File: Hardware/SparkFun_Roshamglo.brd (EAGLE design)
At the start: 33 x 72.4 mm, 43 parts, among them IC1 ATTINY84A, J2 USBPCB, Q1 600mA/40V, U1 IR-Receiver, U3 AP2112K-3.3V

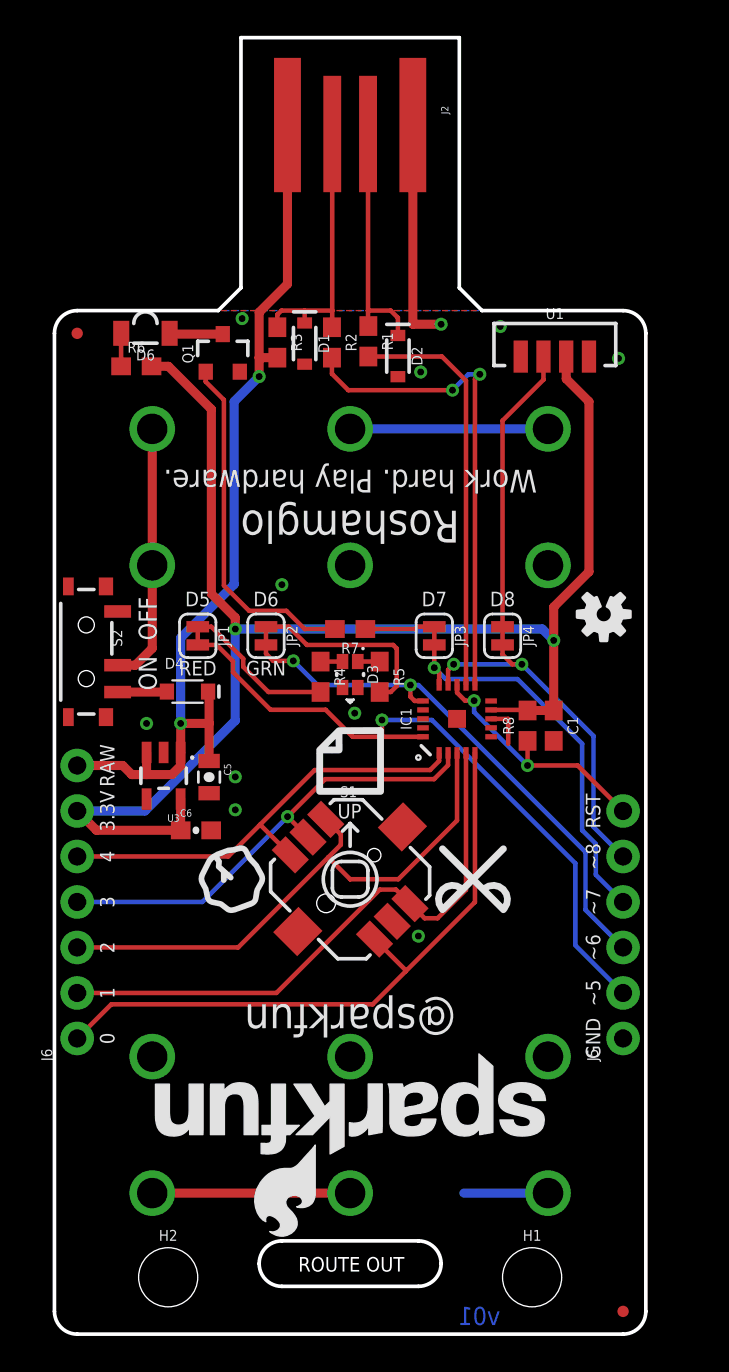
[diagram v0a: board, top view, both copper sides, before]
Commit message: v02 Changes
- Moved IR LED to GPIO 5
- Moved red and green LEDs to GPIO 7 and 8
- Moved IR receiver to GPIO 3
- Moved center switch to GPIO 6
- Increased distance between batteries
- Increased board size to 1.4"
- Added reset switch
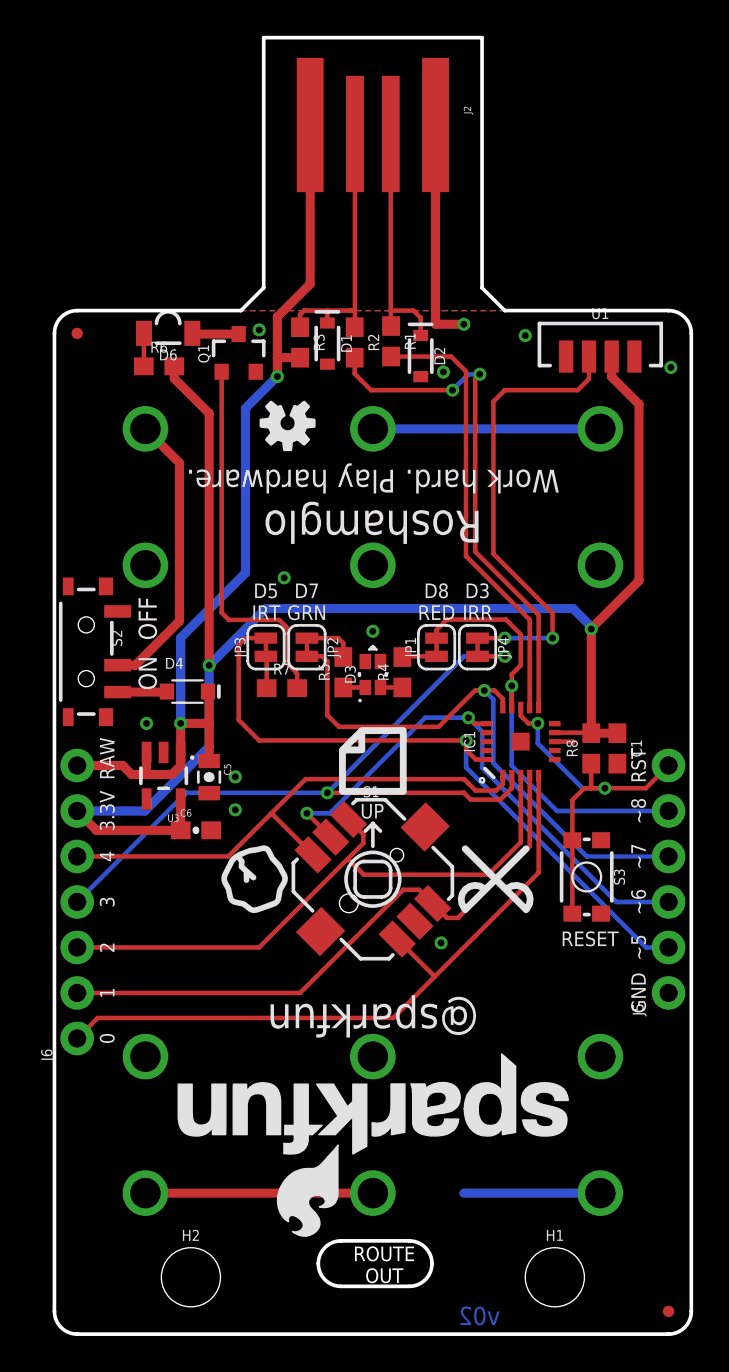
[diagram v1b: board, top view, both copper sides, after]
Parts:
- added S3: (no value), SparkFun-Switches:TACTILE_SWITCH_SMD_4.6X2.8MM
- moved LOGO1 20.6 mm to (13.0, 50.9)
- moved JP1 13.4 mm to (21.3, 38.4), turned to 90 degrees
- moved JP3 9.42 mm to (11.8, 38.4), turned to 90 degrees
- moved R7 5.04 mm to (12.7, 36.1), turned to 0 degrees
- moved R4 4.58 mm to (19.4, 37.0), turned to 90 degrees
- moved C1 3.78 mm to (31.4, 32.7)
- moved IC1 3.78 mm to (26.0, 33.1)
- moved R8 3.78 mm to (30.0, 32.7)
- moved J5 3.59 mm to (34.3, 19.1)
- moved BT3 2.92 mm to (30.5, 29.2)
- moved FD2 2.54 mm to (34.3, 1.27)
- moved U1 2.54 mm to (30.5, 55.9)
- moved JP2 2.37 mm to (14.1, 38.4)
- moved R5 2.05 mm to (16.1, 37.0), turned to 90 degrees
- moved JP4 1.53 mm to (23.6, 38.4)
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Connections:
- net !RESET: now also S3.1, S3.2
- net 3: now also JP4.2; no longer S1.CTR
- net 5: now also JP3.2; no longer JP1.2
- net 6: now also S1.CTR; no longer JP2.2
- net 7: now also JP2.2; no longer JP3.2
- net 8: now also JP1.2; no longer JP4.2
- net GND: now also S3.3, S3.4
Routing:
- net 3: track 26.2 -> 42.5 mm, vias 1 -> 2
- net 7: track 22.1 -> 32.1 mm
- net N$9: track 16.0 -> 25.9 mm, vias 0 -> 2
- net N$8: track 11.0 -> 2.96 mm
- net !RESET: track 14.2 -> 21.4 mm
- net N$7: track 8.63 -> 1.94 mm
- net 3.3V: track 84.0 -> 88.5 mm
- net 4: track 25.3 -> 29.7 mm
- net 8: track 20.0 -> 24.3 mm, vias 2 -> 1
- net 2: track 31.7 -> 34.6 mm
- net N$10: track 3.90 -> 1.82 mm
- net 9: track 23.0 -> 24.8 mm
- net 0: track 36.2 -> 38.0 mm
- net N$13: track 11.0 -> 12.7 mm
- net N$12: track 11.0 -> 12.7 mm
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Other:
- board size 33 x 72.4 mm -> 35.6 x 72.4 mm
- board text added: "D3 IRR"
- board text added: "D5 IRT"
- board text added: "D7 GRN"
- board text added: "D8 RED"
- board text added: "RESET"
- board text added: "Units are in Inches"
- board text added: "v02"
- board text removed: "D5"
- board text removed: "D6"
- board text removed: "D7"
- board text removed: "D8"
- board text removed: "GRN"
- board text removed: "RED"
- board text removed: "v01"

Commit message: Fixed V02 DRC errors
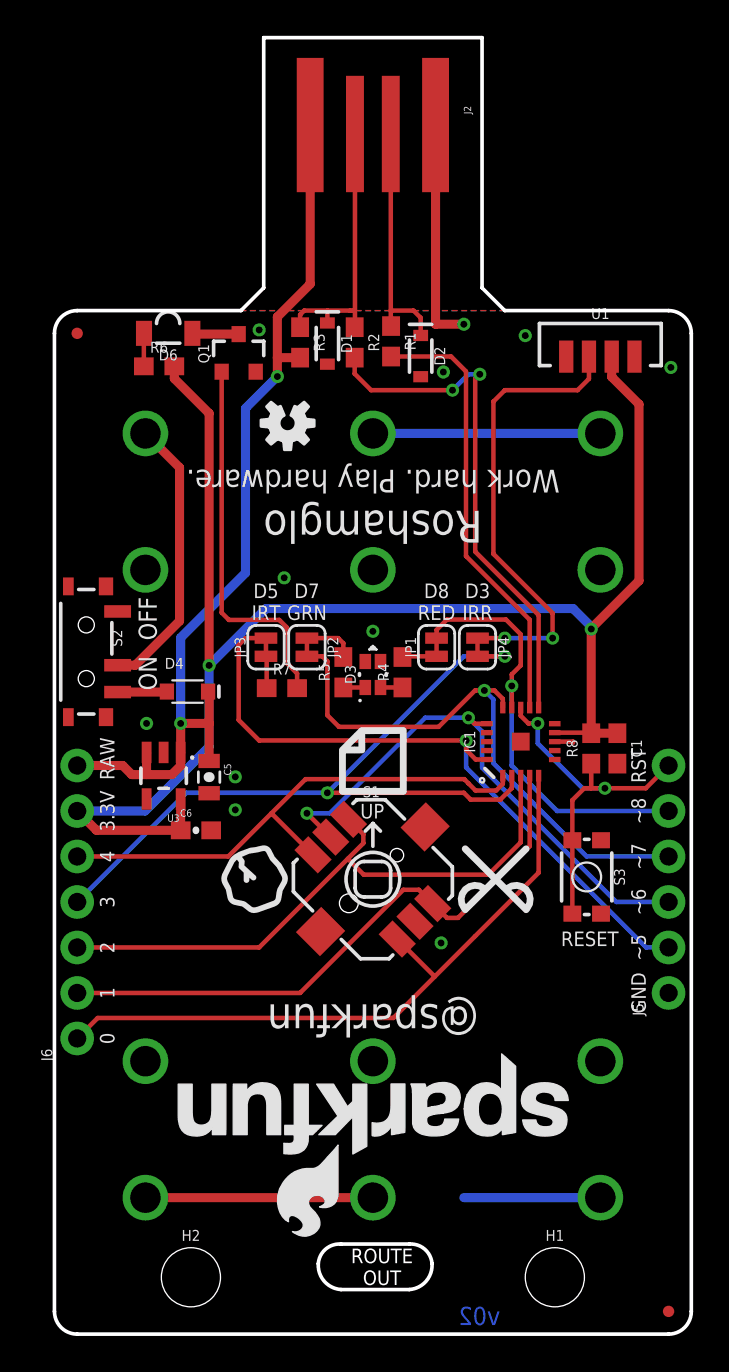
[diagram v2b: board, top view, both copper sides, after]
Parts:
- moved BT1 0.25 mm to (5.08, 29.0)
- moved BT2 0.25 mm to (17.8, 29.0)
- moved BT3 0.25 mm to (30.5, 29.0)
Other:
- outline, holes or cut-outs redrawn
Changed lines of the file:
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@@
 <layer number="31" name="tCream" color="7" fill="4" visible="no" active="yes"/>
 <layer number="32" name="bCream" color="7" fill="5" visible="no" active="yes"/>
-<layer number="39" name="tKeepout" color="4" fill="11" visible="no" active="yes"/>
-<layer number="40" name="bKeepout" color="1" fill="11" visible="no" active="yes"/>
+<layer number="39" name="tKeepout" color="4" fill="11" visible="yes" active="yes"/>
+<layer number="40" name="bKeepout" color="1" fill="11" visible="yes" active="yes"/>
 <layer number="41" name="tRestrict" color="4" fill="10" visible="no" active="yes"/>
 <layer number="42" name="bRestrict" color="1" fill="10" visible="no" active="yes"/>
@@
 <layer number="47" name="Measures" color="7" fill="1" visible="yes" active="yes"/>
 <layer number="51" name="tDocu" color="6" fill="1" visible="yes" active="yes"/>
-<layer number="52" name="bDocu" color="7" fill="1" visible="no" active="yes"/>
+<layer number="52" name="bDocu" color="7" fill="1" visible="yes" active="yes"/>
 <layer number="3" name="Route3" color="4" fill="3" visible="no" active="no"/>
 <layer number="4" name="Route4" color="1" fill="4" visible="no" active="no"/>
@@
 IRR</text>
 <text x="33.02" y="31.75" size="0.8128" layer="21" font="vector" ratio="15" rot="R90" align="bottom-center">RST</text>
-<text x="18.415" y="2.8575" size="0.8128" layer="20" font="vector" ratio="15" align="bottom-center">ROUTE
+<text x="18.288" y="2.7432" size="0.8128" layer="20" font="vector" ratio="15" align="bottom-center">ROUTE
 OUT</text>
 <text x="17.78" y="55.626" size="1.4224" layer="22" font="vector" ratio="15" rot="SMR180" align="bottom-center">Hack me! sfe.io/roshamglo</text>
@@
 <vertex x="23.3934" y="71.374"/>
 </polygon>
-<wire x1="16.002" y1="5.207" x2="19.812" y2="5.207" width="0.2032" layer="20"/>
-<wire x1="19.812" y1="5.207" x2="21.082" y2="3.937" width="0.2032" layer="20" curve="-90"/>
-<wire x1="21.082" y1="3.937" x2="19.812" y2="2.667" width="0.2032" layer="20" curve="-90"/>
-<wire x1="19.812" y1="2.667" x2="16.002" y2="2.667" width="0.2032" layer="20"/>
-<wire x1="16.002" y1="2.667" x2="14.732" y2="3.937" width="0.2032" layer="20" curve="-90"/>
-<wire x1="14.732" y1="3.937" x2="16.002" y2="5.207" width="0.2032" layer="20" curve="-90"/>
+<wire x1="16.002" y1="5.0292" x2="19.812" y2="5.0292" width="0.2032" layer="20"/>
+<wire x1="19.812" y1="5.0292" x2="21.082" y2="3.937" width="0.2032" layer="20" curve="-90"/>
+<wire x1="21.082" y1="3.937" x2="19.812" y2="2.4892" width="0.2032" layer="20" curve="-90"/>
+<wire x1="19.812" y1="2.4892" x2="16.002" y2="2.4892" width="0.2032" layer="20"/>
+<wire x1="16.002" y1="2.4892" x2="14.732" y2="3.937" width="0.2032" layer="20" curve="-90"/>
+<wire x1="14.732" y1="3.937" x2="16.002" y2="5.0292" width="0.2032" layer="20" curve="-90"/>
 <text x="31.496" y="22.479" size="0.8128" layer="21" font="vector" ratio="15" rot="R180">RESET</text>
 <dimension x1="7.62" y1="3.175" x2="0" y2="3.175" x3="3.81" y3="-5.08" textsize="1.016" textratio="15" layer="47" unit="inch" precision="3"/>
@@
 </autorouter>
 <elements>
-<element name="BT1" library="SparkFun-Batteries" package="BATTERY-AAA-KIT" value="1.2V" x="5.08" y="29.21" rot="MR270">
-<attribute name="SF_SKU" value="PRT-12718" x="5.08" y="29.21" size="1.778" layer="28" rot="MR270" display="off"/>
-<attribute name="PROD_ID" value="BATT-08571" x="5.08" y="29.21" size="1.778" layer="28" rot="MR270" display="off"/>
-</element>
-<element name="BT2" library="SparkFun-Batteries" package="BATTERY-AAA-KIT" value="1.2V" x="17.78" y="29.21" rot="MR90">
-<attribute name="SF_SKU" value="PRT-12718" x="17.78" y="29.21" size="1.778" layer="28" rot="MR90" display="off"/>
-<attribute name="PROD_ID" value="BATT-08571" x="17.78" y="29.21" size="1.778" layer="28" rot="MR90" display="off"/>
-</element>
-<element name="BT3" library="SparkFun-Batteries" package="BATTERY-AAA-KIT" value="1.2V" x="30.48" y="29.21" rot="MR270">
-<attribute name="SF_SKU" value="PRT-12718" x="30.48" y="29.21" size="1.778" layer="28" rot="MR270" display="off"/>
-<attribute name="PROD_ID" value="BATT-08571" x="30.48" y="29.21" size="1.778" layer="28" rot="MR270" display="off"/>
+<element name="BT1" library="SparkFun-Batteries" package="BATTERY-AAA-KIT" value="1.2V" x="5.08" y="28.956" rot="MR270">
+<attribute name="SF_SKU" value="PRT-12718" x="5.08" y="28.956" size="1.778" layer="28" rot="MR270" display="off"/>
+<attribute name="PROD_ID" value="BATT-08571" x="5.08" y="28.956" size="1.778" layer="28" rot="MR270" display="off"/>
+</element>
+<element name="BT2" library="SparkFun-Batteries" package="BATTERY-AAA-KIT" value="1.2V" x="17.78" y="28.956" rot="MR90">
+<attribute name="SF_SKU" value="PRT-12718" x="17.78" y="28.956" size="1.778" layer="28" rot="MR90" display="off"/>
+<attribute name="PROD_ID" value="BATT-08571" x="17.78" y="28.956" size="1.778" layer="28" rot="MR90" display="off"/>
+</element>
+<element name="BT3" library="SparkFun-Batteries" package="BATTERY-AAA-KIT" value="1.2V" x="30.48" y="28.956" rot="MR270">
+<attribute name="SF_SKU" value="PRT-12718" x="30.48" y="28.956" size="1.778" layer="28" rot="MR270" display="off"/>
+<attribute name="PROD_ID" value="BATT-08571" x="30.48" y="28.956" size="1.778" layer="28" rot="MR270" display="off"/>
 </element>
 <element name="C1" library="SparkFun-Capacitors" package="0603" value="0.1uF" x="31.4325" y="32.7025" rot="R270">
@@
 <via x="10.0965" y="31.115" extent="1-16" drill="0.381"/>
 <via x="5.1435" y="34.0995" extent="1-16" drill="0.381"/>
-<wire x1="30.48" y1="7.874" x2="22.86" y2="7.874" width="0.508" layer="16"/>
+<wire x1="30.48" y1="7.62" x2="22.86" y2="7.62" width="0.508" layer="16"/>
 <wire x1="21.28" y1="67.51" x2="21.28" y2="56.388" width="0.508" layer="1"/>
 <wire x1="21.28" y1="56.388" x2="22.86" y2="56.388" width="0.508" layer="1"/>
@@
 <contactref element="BT1" pad="PWR@1"/>
 <contactref element="S2" pad="2"/>
-<wire x1="5.461" y1="38.292925" x2="4.518075" y2="37.35" width="0.508" layer="1"/>
 <wire x1="4.518075" y1="37.35" x2="3.528" y2="37.35" width="0.508" layer="1"/>
-<wire x1="5.461" y1="38.292925" x2="6.985" y2="39.816925" width="0.508" layer="1"/>
-<wire x1="6.985" y1="39.816925" x2="6.985" y2="48.641" width="0.508" layer="1"/>
-<wire x1="6.985" y1="48.641" x2="5.08" y2="50.546" width="0.508" layer="1"/>
+<wire x1="4.518075" y1="37.35" x2="6.985" y2="39.816925" width="0.508" layer="1"/>
+<wire x1="5.08" y1="50.292" x2="6.985" y2="48.387" width="0.508" layer="1"/>
+<wire x1="6.985" y1="48.387" x2="6.985" y2="39.816925" width="0.508" layer="1"/>
 </signal>
 <signal name="N$12">
 <contactref element="BT1" pad="GND@1"/>
 <contactref element="BT2" pad="PWR@1"/>
-<wire x1="17.78" y1="7.874" x2="5.08" y2="7.874" width="0.508" layer="1"/>
+<wire x1="17.78" y1="7.62" x2="5.08" y2="7.62" width="0.508" layer="1"/>
 </signal>
 <signal name="N$13">
 <contactref element="BT2" pad="GND@1"/>
 <contactref element="BT3" pad="PWR@1"/>
-<wire x1="30.48" y1="50.546" x2="17.78" y2="50.546" width="0.508" layer="16"/>
+<wire x1="30.48" y1="50.292" x2="17.78" y2="50.292" width="0.508" layer="16"/>
 </signal>
 <signal name="VIN">

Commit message: v02 changes
Added power LED
Added external parallel resistor
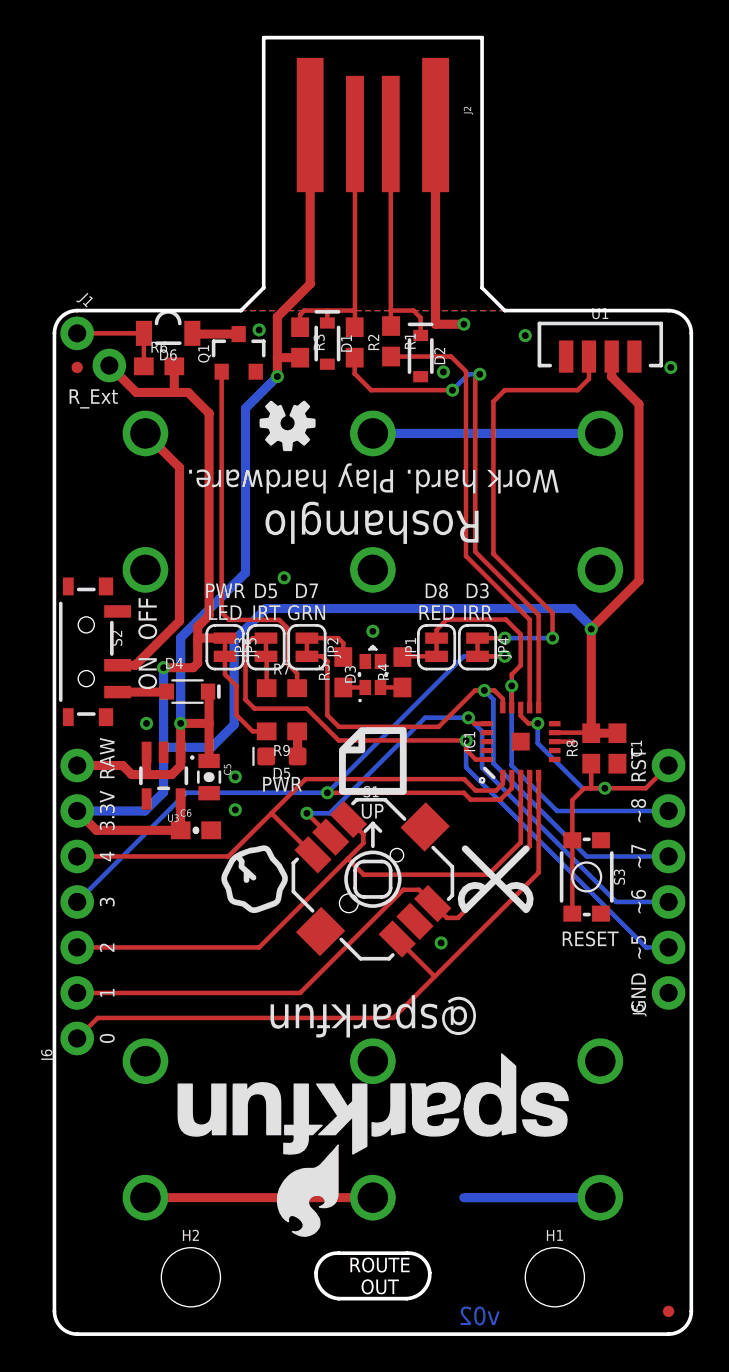
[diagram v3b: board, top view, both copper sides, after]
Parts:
- added D5: RED, SparkFun-LED:LED-0603
- added J1: R_Ext, SparkFun-Connectors:1X02_NO_SILK
- added JP5: (no value), SparkFun-Jumpers:SMT-JUMPER_2_NC_TRACE_SILK
- added R9: 1k, SparkFun-Resistors:0603
- moved FD1 1.91 mm to (1.27, 54.0)
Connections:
- new net N$11: JP5.2, R9.2
- new net N$14: D6.2, J1.1, R6.1
- net 3.3V: now also J1.2, JP5.1
- net GND: now also D5.C
- net N$1: now also D5.A, R9.1; no longer D6.2, R6.1
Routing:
- net 3.3V: track 88.5 -> 103.0 mm
- net N$11: track 0.00 -> 5.61 mm
- net N$14: track 0.00 -> 5.57 mm
- net 5: track 37.9 -> 36.5 mm
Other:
- outline, holes or cut-outs redrawn
- board text added: "PWR"
- board text added: "PWR LED"
- board text added: "R_Ext"

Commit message: v02 changes
- Switch back to old size for lanyard clip
- Changed the "@" to proportional
- Moved pin 4 to other header to leave more room for battery terminal
soldering
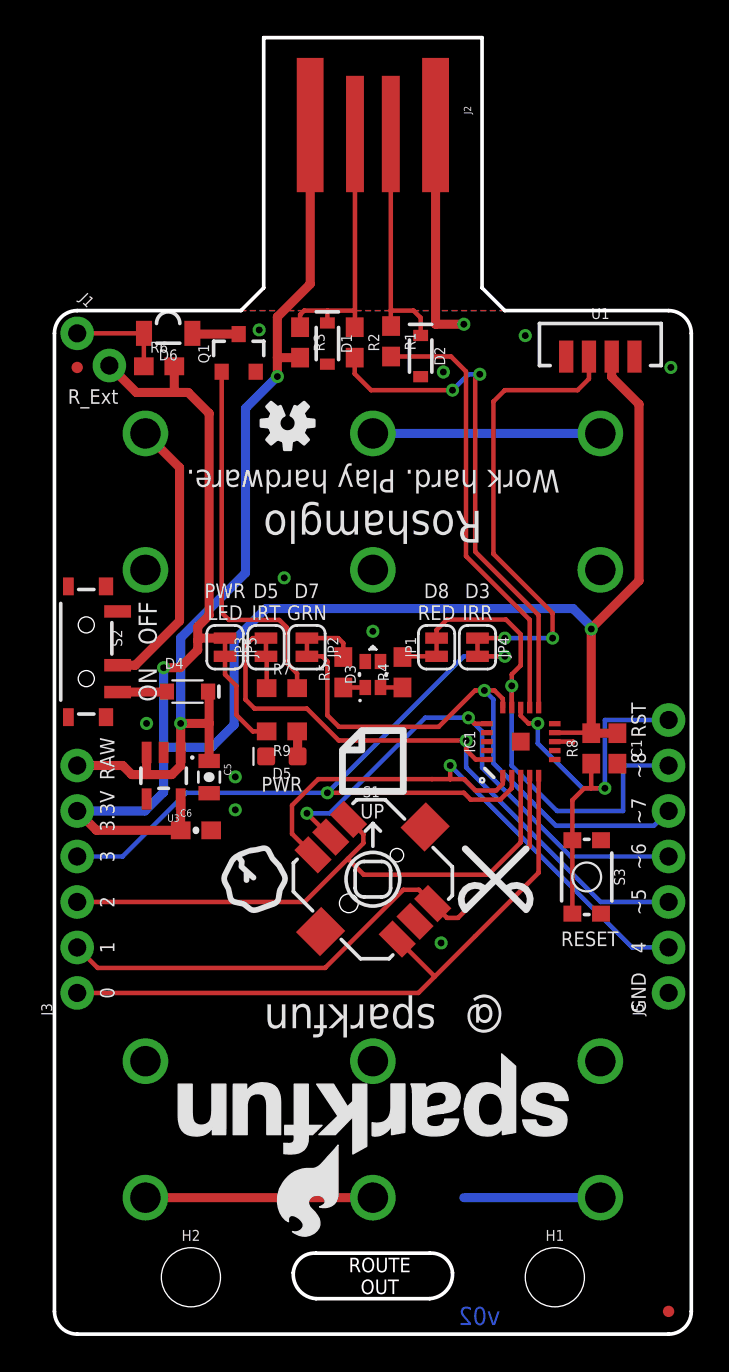
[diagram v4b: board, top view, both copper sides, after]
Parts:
- removed J6: (no value), SparkFun-Connectors:1X07_NO_SILK
- added J3: (no value), SparkFun-Connectors:1X06_NO_SILK
- J5: device SparkFun-Connectors:1X06_NO_SILK -> SparkFun-Connectors:1X07_NO_SILK
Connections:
- net !RESET: now also J5.7; no longer J5.6
- net 0: now also J3.1; no longer J6.1
- net 1: now also J3.2; no longer J6.2
- net 2: now also J3.3; no longer J6.3
- net 3: now also J3.4; no longer J6.4
- net 3.3V: now also J3.5; no longer J6.6
- net 4: now also J5.2; no longer J6.5
- net 5: now also J5.3; no longer J5.2
- net 6: now also J5.4; no longer J5.3
- net 7: now also J5.5; no longer J5.4
- net 8: now also J5.6; no longer J5.5
- net VIN: now also J3.6; no longer J6.7
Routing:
- net 4: track 29.7 -> 33.7 mm, vias 0 -> 1
- net !RESET: track 21.4 -> 24.7 mm
- net 8: track 24.3 -> 26.8 mm
- net 3: track 42.5 -> 41.4 mm
- net 6: track 30.9 -> 29.8 mm
- net 5: track 36.5 -> 35.4 mm
- net 2: track 34.6 -> 33.5 mm
- net 0: track 38.0 -> 36.9 mm
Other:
- outline, holes or cut-outs redrawn
- board text added: "@"
- board text added: "sparkfun"
- board text removed: "@sparkfun"
